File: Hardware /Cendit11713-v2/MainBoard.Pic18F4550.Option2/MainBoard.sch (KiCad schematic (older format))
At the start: 91 parts, among them CON1 POWER_BUS, CON2 ICSP_CON, CON3 USB_CON, J1 RESET_CON, J2 SATA_PLUG _22P_SMT, J4 SATA_PLUG _22P_SMT, P1 DEBUG_HEADER_21P, P2 DEBUG_HEADER_21P, Q1 2N2222-SOT23, U1 PIC18F4550-I/P, U3 PCF85263A, Y1 Crystal, Y2 32.768KHZ

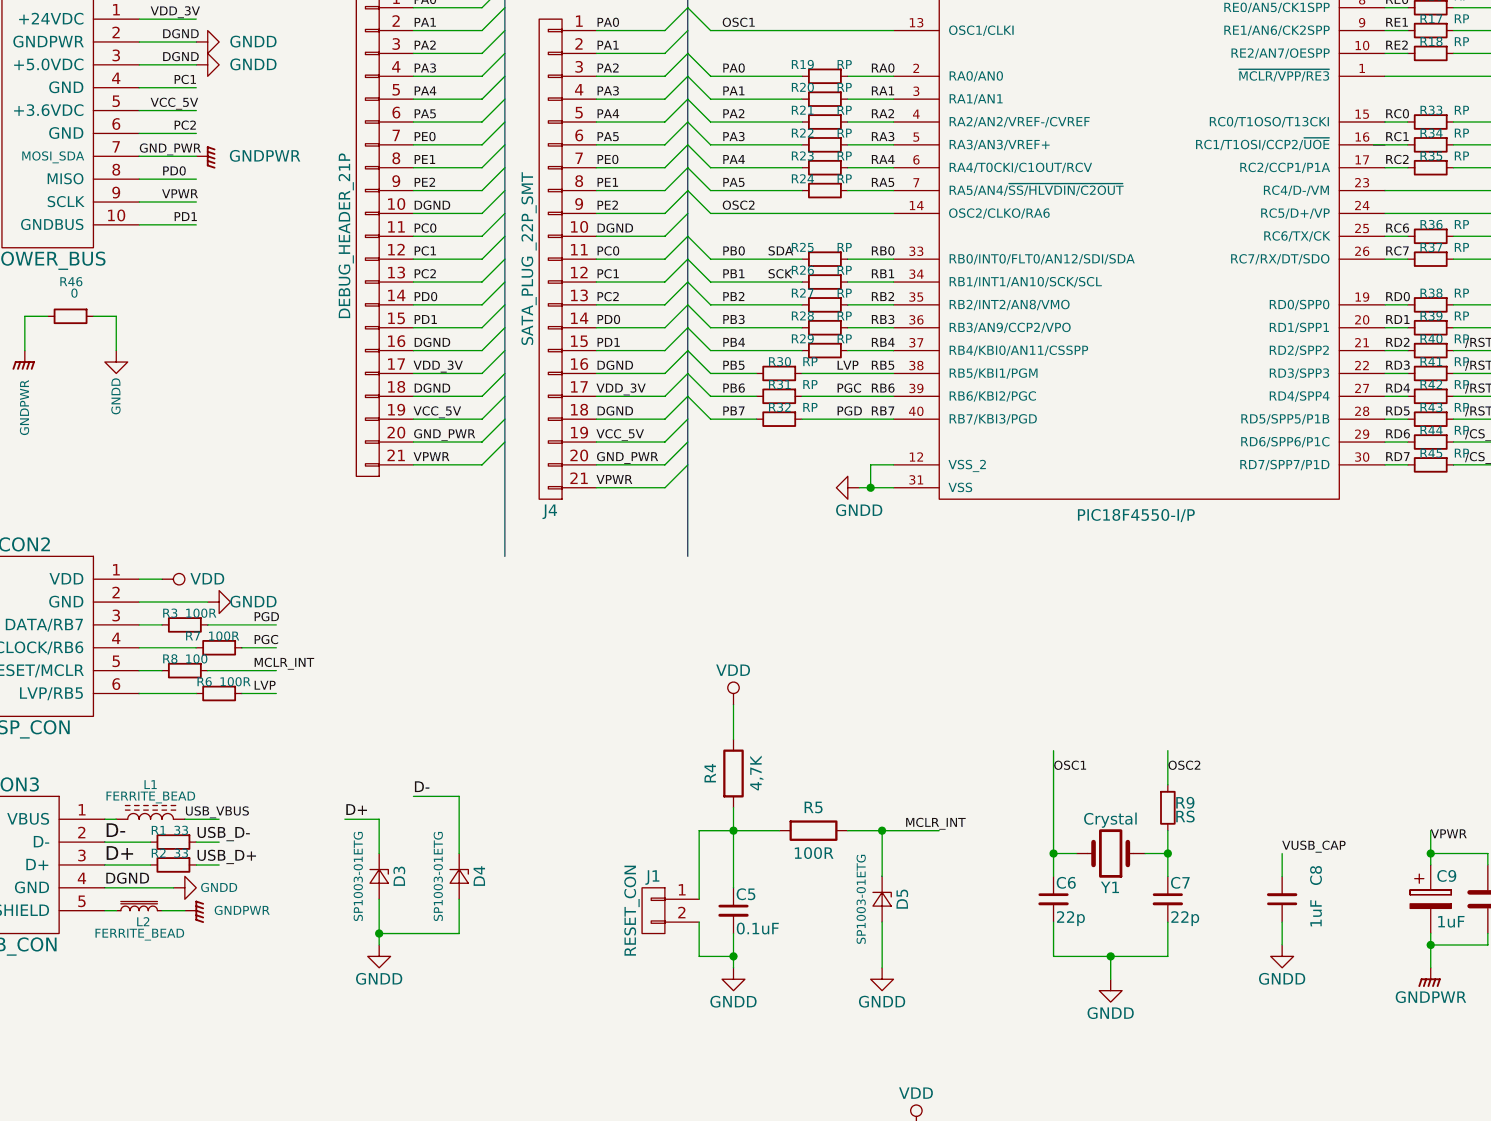
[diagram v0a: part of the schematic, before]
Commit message: En Cendit11713 + CenditLab respaldo
  - Se revisan tarjetas
  - Correccion en PCB GPIB
  - Se inicia tarjeta madre en una pieza (MainBoard.OnePiece)
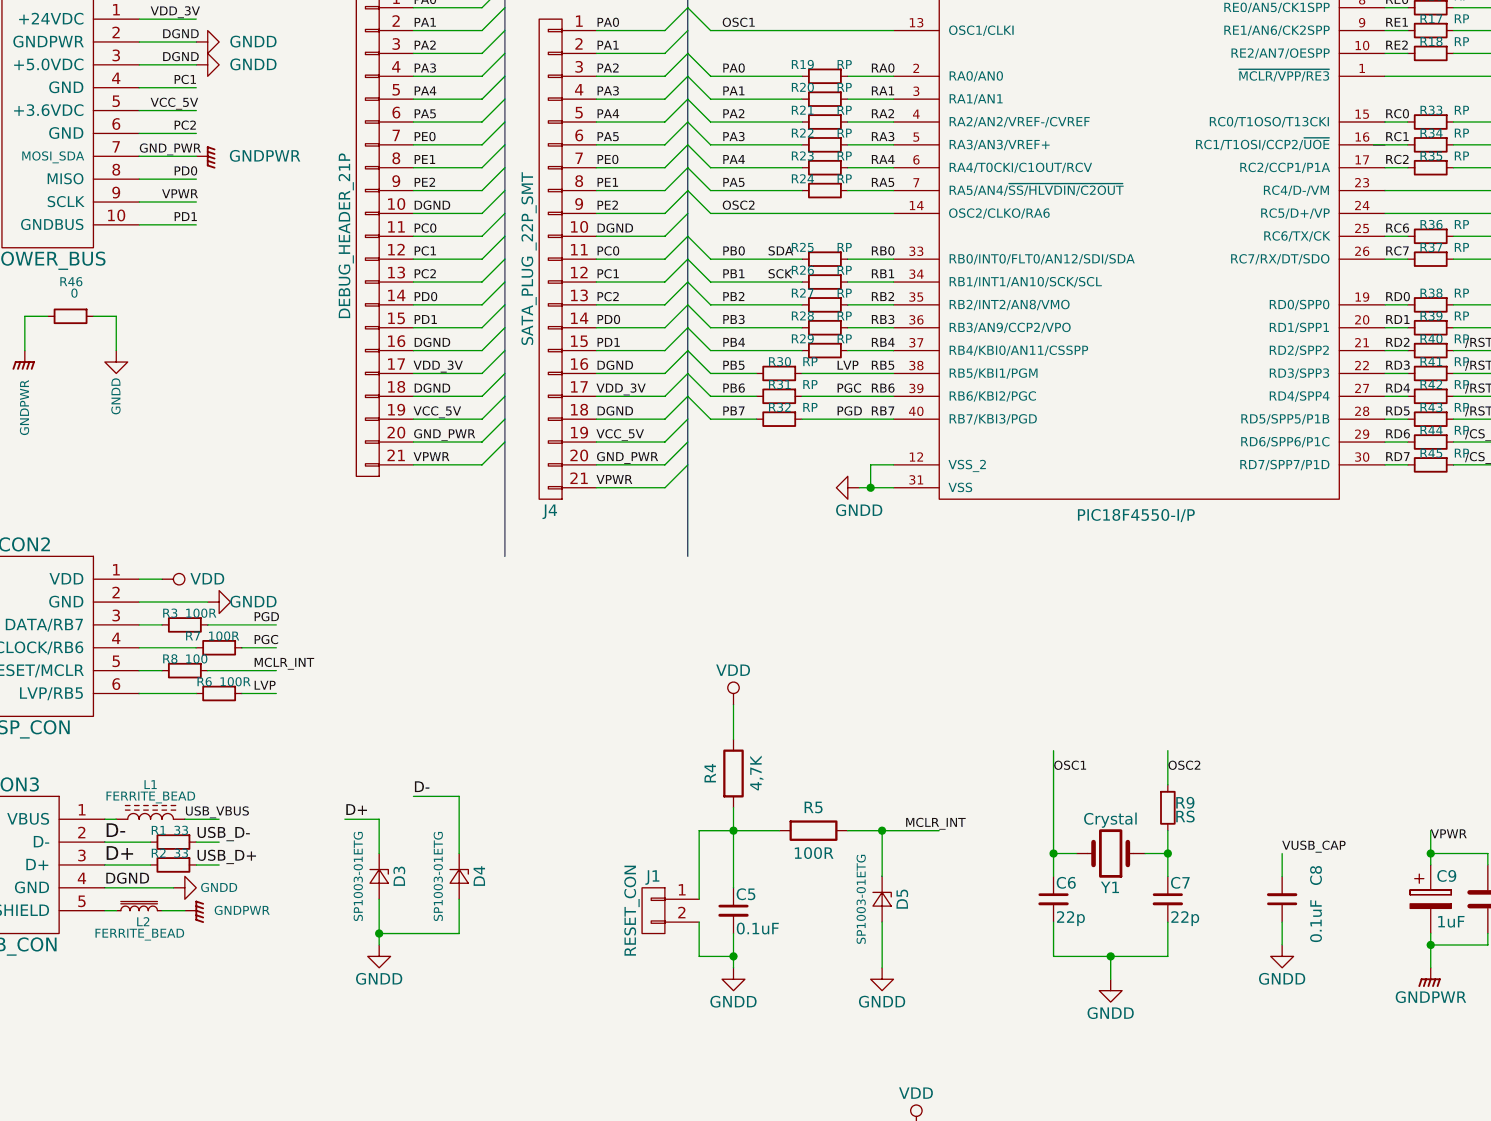
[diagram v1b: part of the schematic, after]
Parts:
- C8: value 1uF -> 0.1uF
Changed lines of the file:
@@
 P 6500 5150
 F 0 "C8" V 6350 5000 50  0000 L CNN
-F 1 "1uF" V 6350 5150 50  0000 L CNN
+F 1 "0.1uF" V 6350 5150 50  0000 L CNN
 F 2 "Capacitors_SMD:C_1206_HandSoldering" H 6500 5150 50  0001 C CNN
 F 3 "" H 6500 5150 50  0001 C CNN
@@
 Text Label 1650 2200 0    39   ~ 0
 PD1
-Text Label 1600 2000 0    39   ~ 0
+Text Label 1650 2000 0    39   ~ 0
 PD0
 Text Label 1650 1800 0    39   ~ 0
